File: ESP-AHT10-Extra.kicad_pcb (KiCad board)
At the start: 2 copper layers, 38.2 x 20.8 mm, 26 parts, among them J1 USB, SW1 RESET, SW2 PROG, U1 CH330N, U2 HT7233, U3 ESP-12, U4 AHT10, U5 USBLC6-2SC6

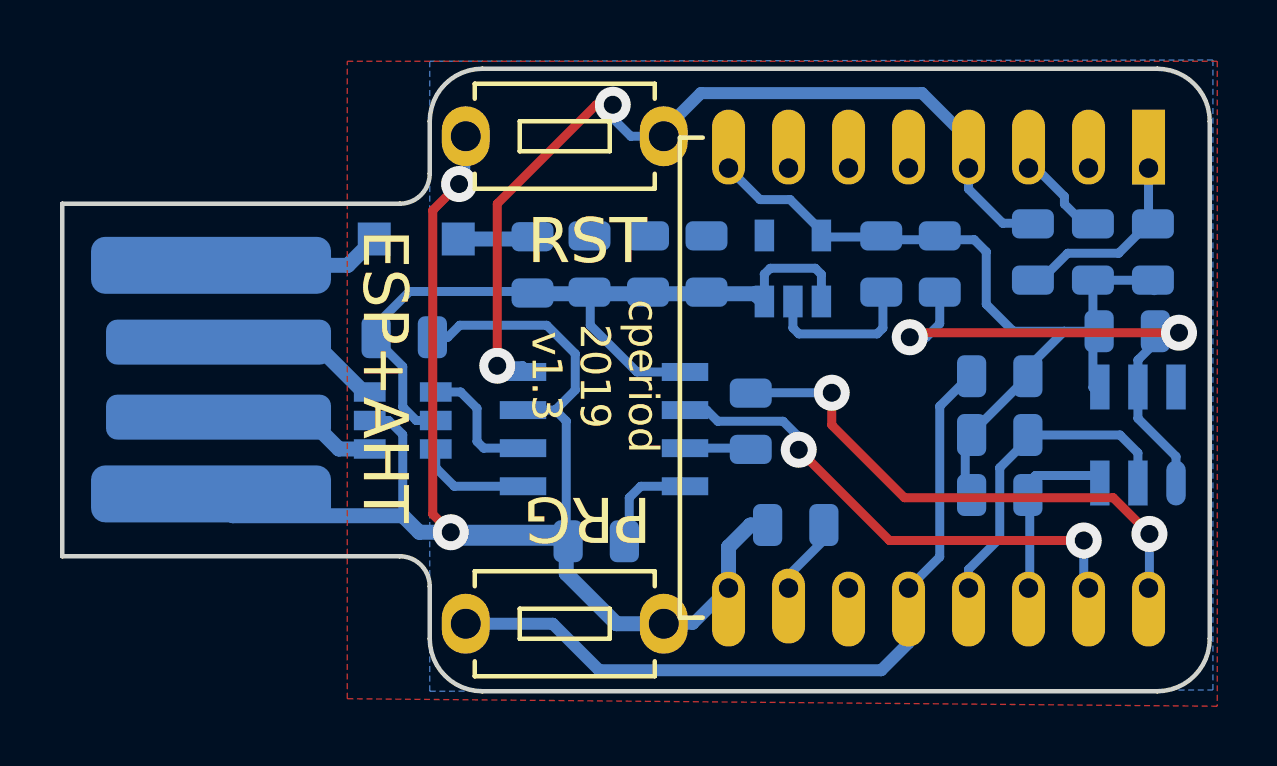
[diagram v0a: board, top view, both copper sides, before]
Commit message: Connecting the CH330N to RESET is a bad idea when it's running on bus voltage.
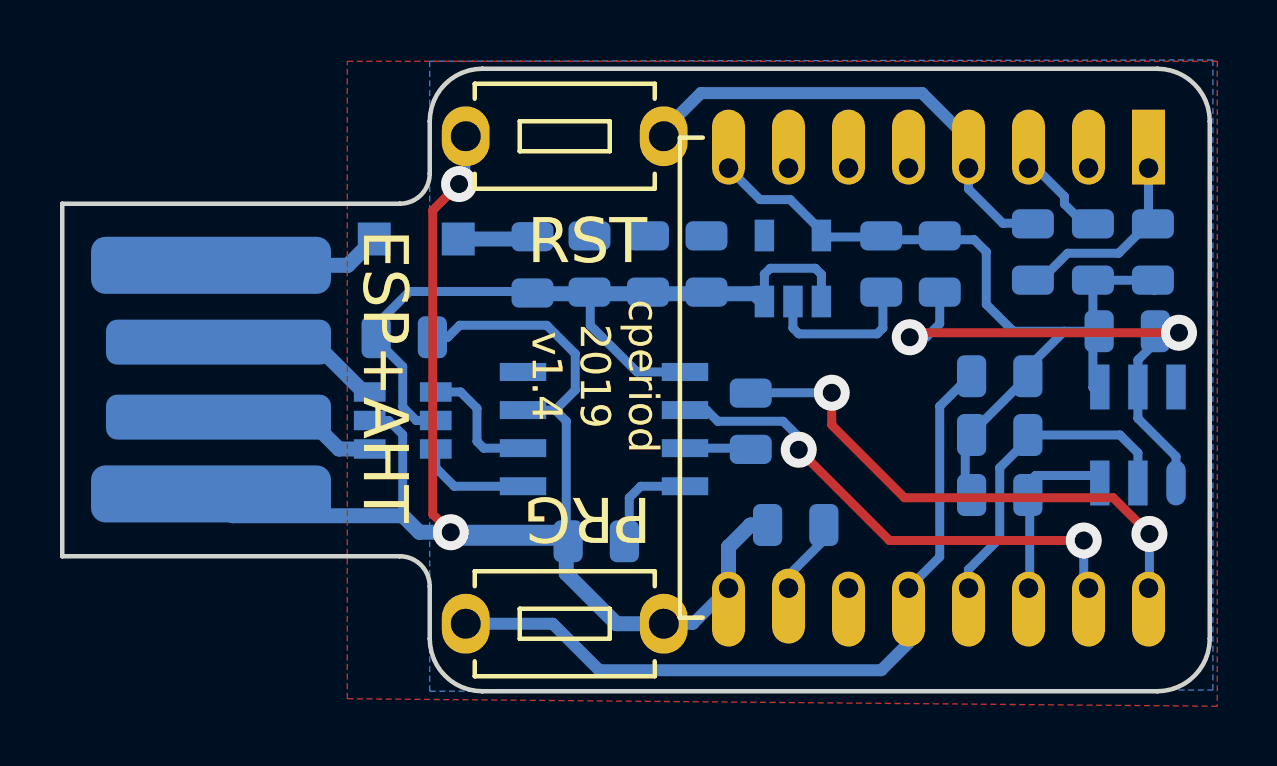
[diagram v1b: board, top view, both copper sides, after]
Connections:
- U1 pad 4: RESET -> (no net)
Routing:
- net RESET: track 29.8 -> 15.7 mm, vias 2 -> 0
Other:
- board text added: "cperiod 2019 v1.4"
- board text removed: "cperiod 2019 v1.3"

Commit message: remove the RESET label
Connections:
- net RESET renamed Net-(R2-Pad2)
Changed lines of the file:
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@@
   (net 18 "Net-(R8-Pad2)")
   (net 19 "Net-(D1-Pad1)")
-  (net 20 RESET)
+  (net 20 "Net-(R2-Pad2)")
   (net_class Default "This is the default net class."
     (clearance 0.35)
@@
     (add_net "Net-(R1-Pad2)")
     (add_net "Net-(R2-Pad1)")
+    (add_net "Net-(R2-Pad2)")
     (add_net "Net-(R4-Pad1)")
     (add_net "Net-(R5-Pad2)")
     (add_net "Net-(R8-Pad2)")
-    (add_net RESET)
     (add_net SCL)
     (add_net SDA)
@@
       (net 5 "Net-(R1-Pad2)"))
     (pad 4 thru_hole oval (at 0 6 270) (size 2.5 1.1) (drill 0.65 (offset -0.7 0)) (layers *.Cu *.Mask F.SilkS)
-      (net 20 RESET))
+      (net 20 "Net-(R2-Pad2)"))
     (pad 5 thru_hole oval (at 0 8 270) (size 2.5 1.1) (drill 0.65 (offset -0.7 0)) (layers *.Cu *.Mask F.SilkS))
     (pad 6 thru_hole oval (at 0 10 270) (size 2.5 1.1) (drill 0.65 (offset -0.7 0)) (layers *.Cu *.Mask F.SilkS))
@@
       (net 2 GND))
     (pad 1 thru_hole oval (at 0 3.3 90) (size 2 1.6) (drill 1) (layers *.Cu *.Mask)
-      (net 20 RESET))
+      (net 20 "Net-(R2-Pad2)"))
   )
   (module "CPB:Tact Switch 6mmx3.5mm C318817" (layer F.Cu)
@@
       (net 6 "Net-(R2-Pad1)"))
     (pad 2 smd roundrect (at 0.9375 0 90) (size 0.975 1.4) (layers B.Cu B.Paste B.Mask) (roundrect_rratio 0.25)
-      (net 20 RESET))
+      (net 20 "Net-(R2-Pad2)"))
     (model ${KISYS3DMOD}/Resistor_SMD.3dshapes/R_0805_2012Metric.wrl
       (at (xyz 0 0 0))

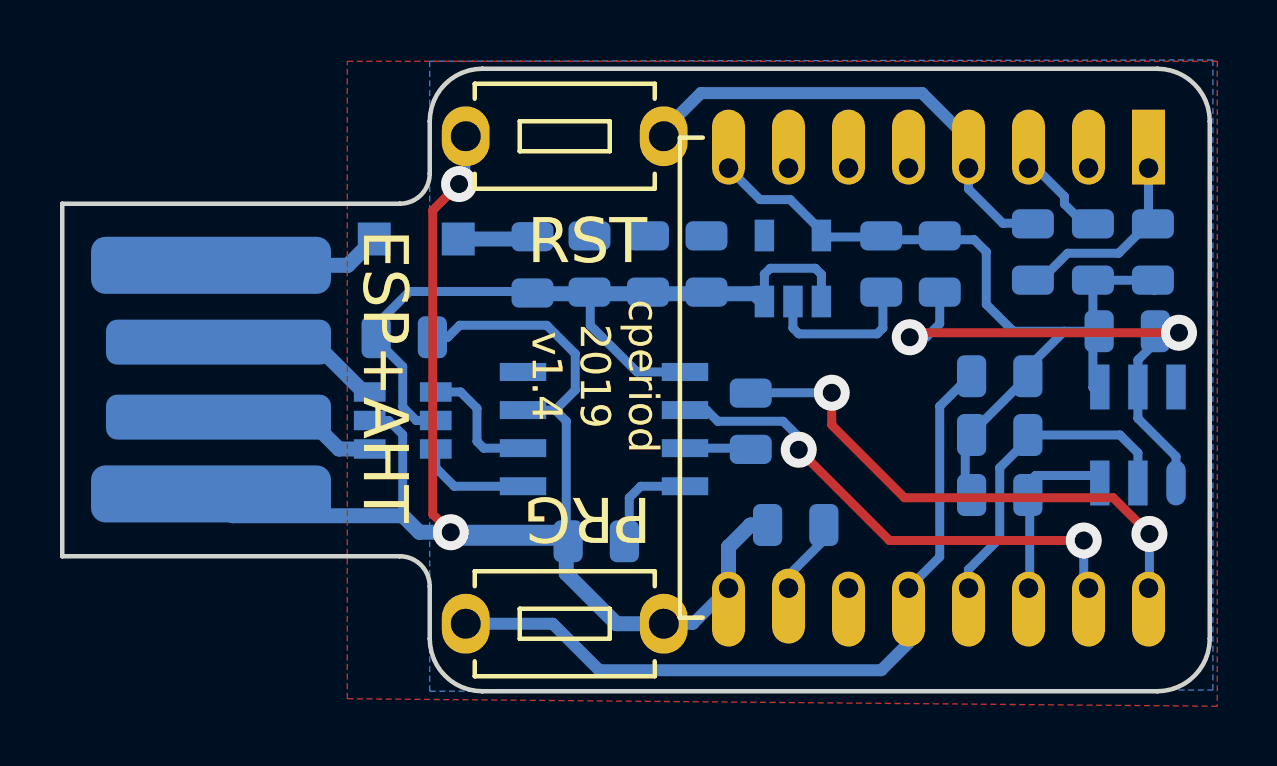
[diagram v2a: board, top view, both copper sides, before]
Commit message: drop that extra 10uF cap. Aside from no longer being needed, this was probably keeping us beyond the USB spec.
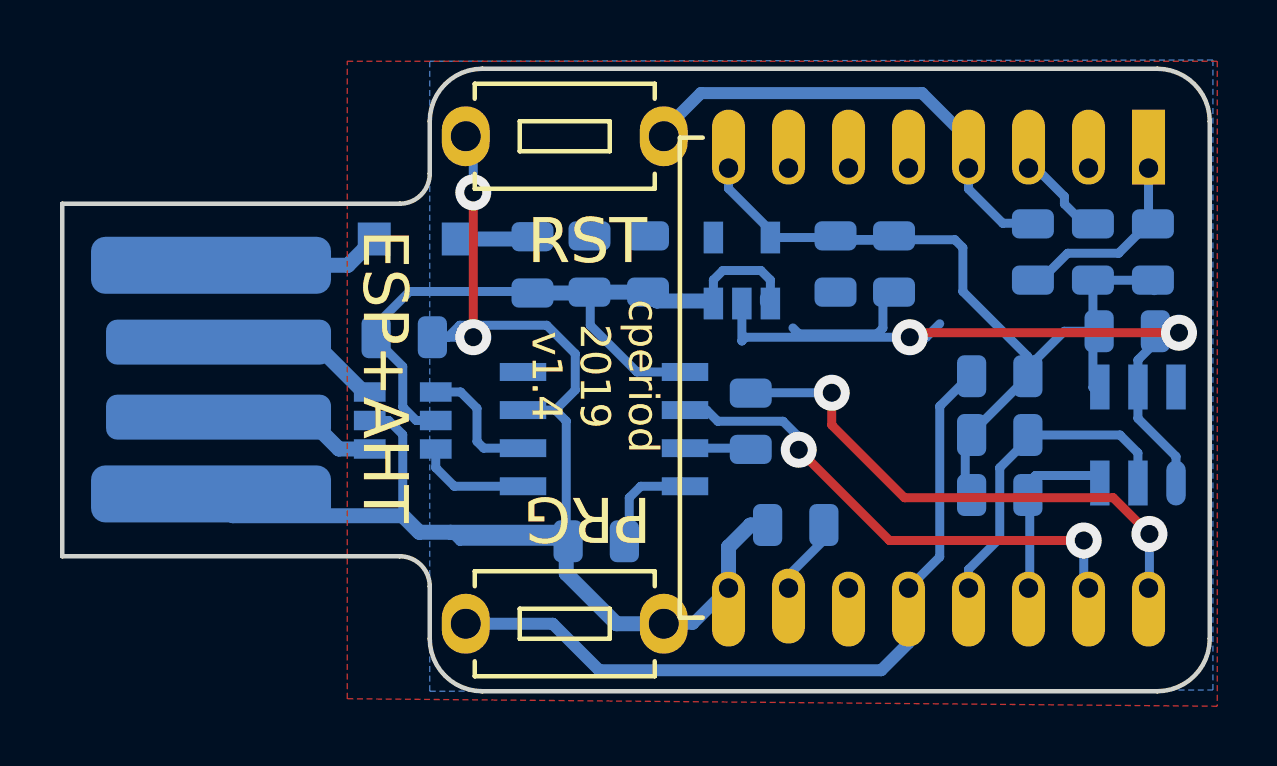
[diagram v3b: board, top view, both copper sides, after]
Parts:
- removed C8: 10u, Capacitor_SMD:C_0805_2012Metric
- moved U2 1.70 mm to (152.7, 93.7)
- moved C1 1.52 mm to (155.8, 93.5)
- moved C4 1.52 mm to (157.7, 93.5)
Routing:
- net 5V: track 27.0 -> 25.1 mm
- net 3V3: track 28.7 -> 29.7 mm

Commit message: cleanup some ground plane concerns swap to a SOT-23-3 footprint regulator bump rev to 1.5
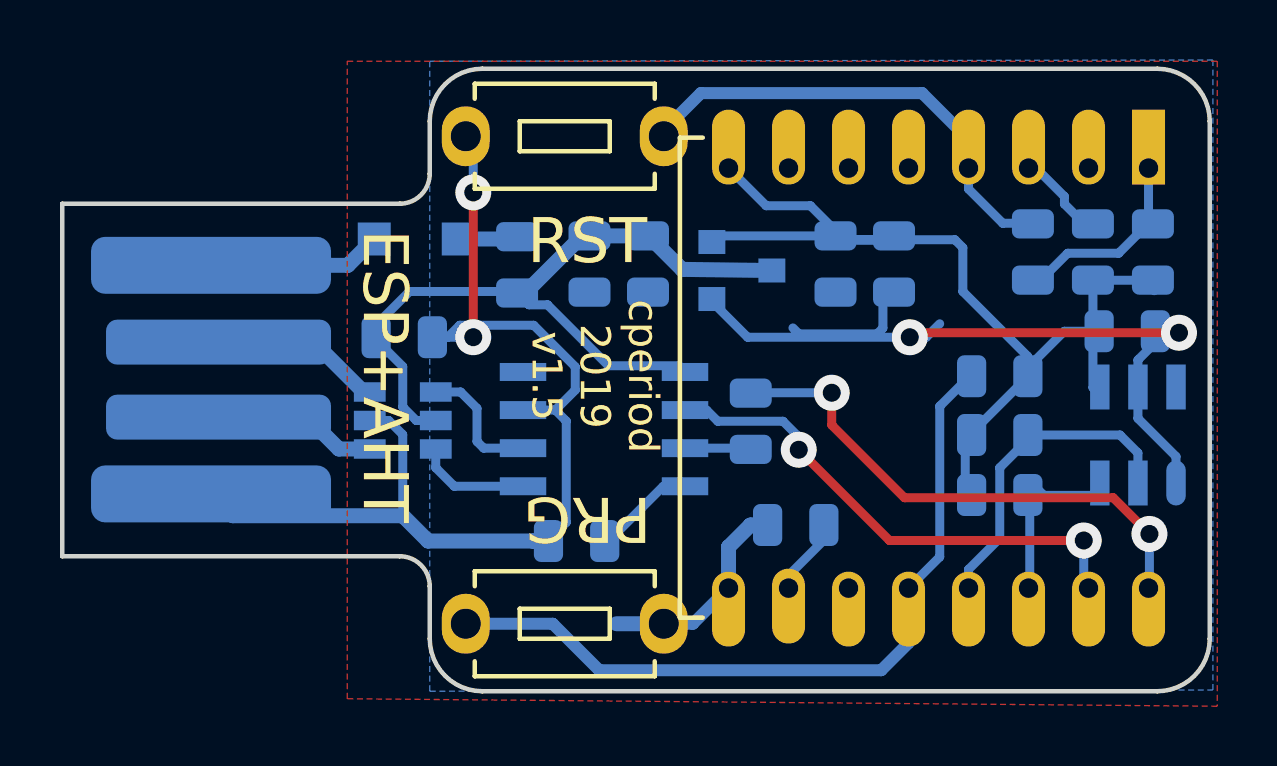
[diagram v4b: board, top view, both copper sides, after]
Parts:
- U2: footprint Package_TO_SOT_SMD:SOT-23-5 -> Package_TO_SOT_SMD:SOT-23
- moved C6 0.66 mm to (147.1, 102.7)
- moved F1 0.51 mm to (145.2, 93.5)
- turned C2 to 270 degrees
- turned C3 to 270 degrees
- turned U2 to 0 degrees
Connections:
- U2 pad 1: 5V -> GND
- U2 pad 2: GND -> 3V3
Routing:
- net GND: track 79.3 -> 71.2 mm
- net 3V3: track 29.7 -> 33.5 mm
- net 5V: track 25.1 -> 26.2 mm
- net SCL: track 5.54 -> 6.17 mm
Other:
- board text added: "cperiod 2019 v1.5"
- board text removed: "cperiod 2019 v1.4"

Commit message: Add a LTR-303 ambient light sensor
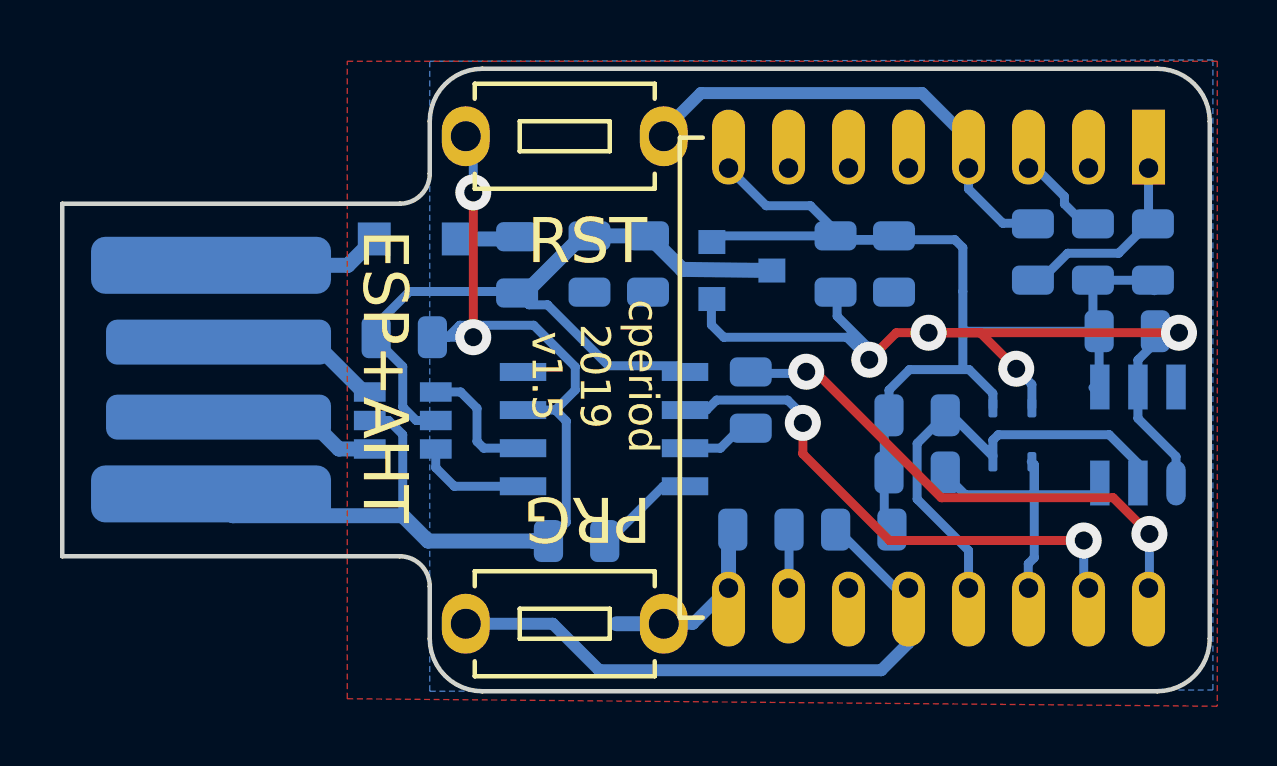
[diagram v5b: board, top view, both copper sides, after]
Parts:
- added U6: LTR-303ALS-01, CPB:Lite-On_LTR-303ALS-01_NoIntNoNc, B.Cu at (161.7, 99.2)
- moved R5 6.83 mm to (156.7, 102.4)
- moved R7 2.85 mm to (158.5, 100.5)
- moved R6 2.83 mm to (158.5, 98.6)
- moved R4 1.17 mm to (153.3, 102.4)
- moved R8 0.71 mm to (152.9, 98.0)
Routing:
- net SCL: track 6.17 -> 11.5 mm
- net 3V3: track 33.5 -> 38.8 mm
- net SDA: track 10.3 -> 15.5 mm
- net Net-(R5-Pad2): track 25.5 -> 20.8 mm
- net GND: track 71.2 -> 73.6 mm, vias 4 -> 6
- net eRX: track 17.0 -> 17.8 mm
- net Net-(R4-Pad1): track 2.65 -> 1.96 mm
